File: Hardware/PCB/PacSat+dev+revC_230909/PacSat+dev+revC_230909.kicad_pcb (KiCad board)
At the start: 6 copper layers, 92 x 92 mm, 333 parts, among them J2 CONN_02X05, J801 Conn_02x05_Odd_Even, P101 U_FL, P601 U_FL, P651 Conn_04x26_Pin, P702 U_FL, P703 U_FL, Q601 SAV-331+, Q701 ATF05MS004NT1, T601 ADT4-1WT+, U156 AX5043, U2 TMS570LS0914PGE, U201 RFShield_OnePiece, U205 AX5043, U206 TLP3905, U26 DS28E83Q+T, U28 MAX31331TETB+, U29 MAX31725MTA+, U30 MAX31725MTA+, U301 RFShield_OnePiece, U305 AX5043, U401 RFShield_OnePiece, U405 AX5043, U501 RFShield_OnePiece, U505 AX5043, U602 LT6657AHMS8-2.5, U604 RBP-140+, U652 CDCLVC1106, U701 RFShield_OnePiece, U703 4n7, U705 SXBP-425+, U76 MR25H40CDE, U77 MR25H40CDE, U78 MR25H40CDE, U79 MR25H40CDE, U86 TPS7A7001DDA, U87 MAX1556AEBT+, U88 MAX1556A, U89 TPS22917DBV, U90 STWD100NYWY3F, U91 MAX4995ALAUT, U92 MAX4995ALAUT, U93 MAX4995ALAUT, U94 MAX4995ALAUT, U95 STWD100NYWY3F, Y26 AB26T-32.768KHZ-6B, Y601 588S160X2CAT

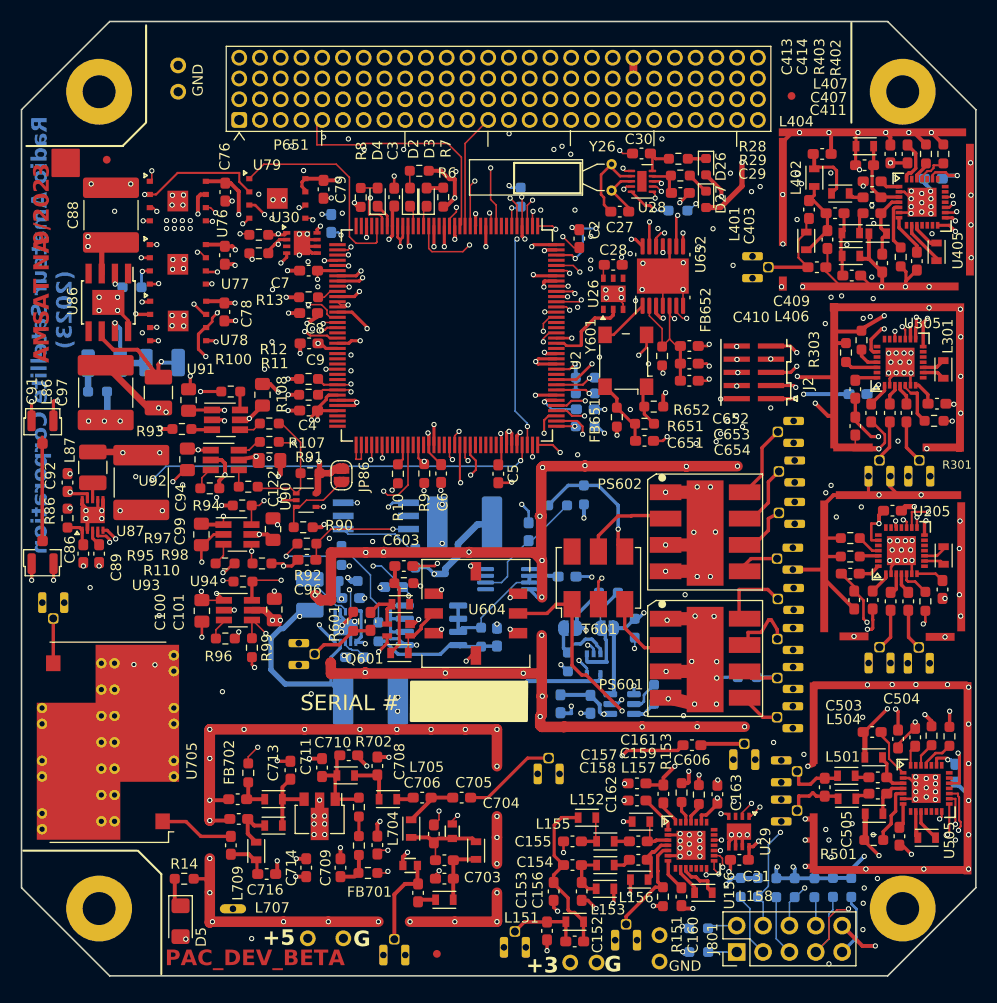
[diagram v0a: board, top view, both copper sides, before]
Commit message: Changed schematic to add Select lines for each AX5043 on the CPU.
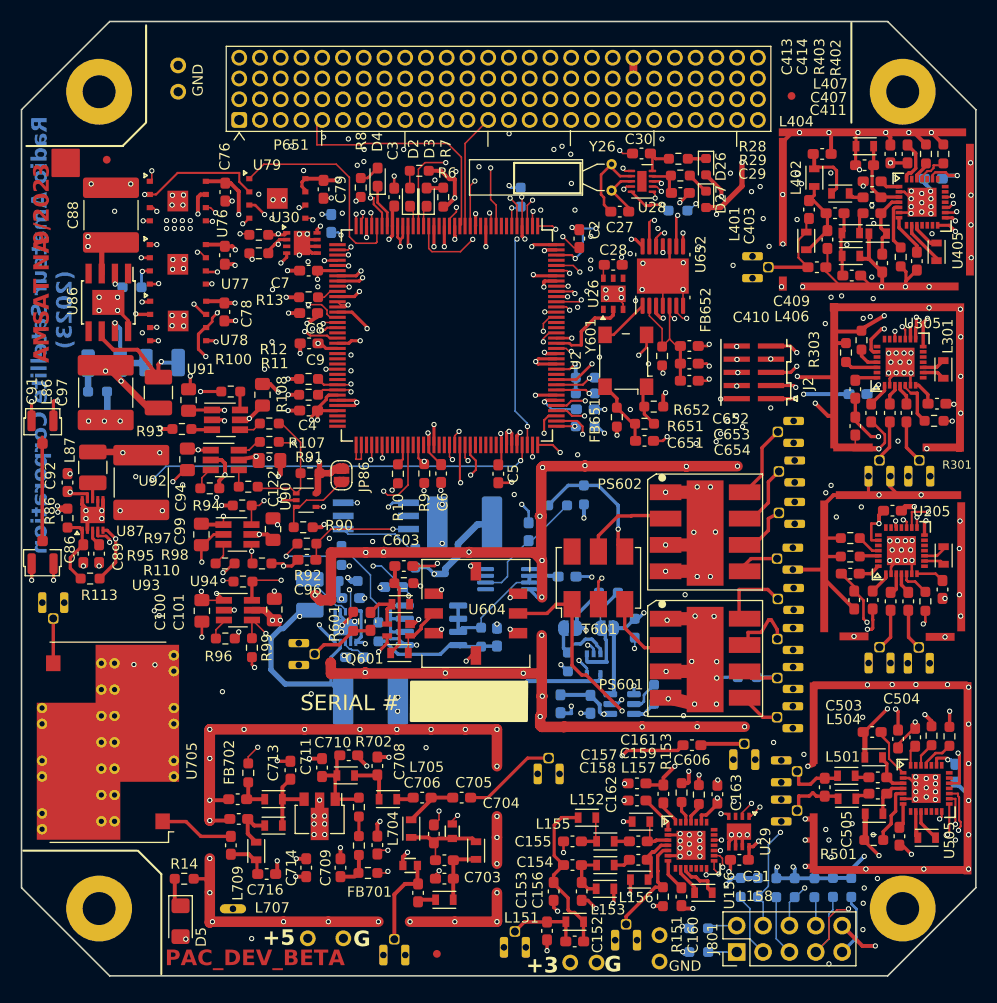
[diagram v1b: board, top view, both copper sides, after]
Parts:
- added R113: 3.8K, Resistor_SMD:R_0603_1608Metric_Pad0.98x0.95mm_HandSolder, F.Cu at (156.6, 111.7)
- moved D4 1.93 mm to (184.3, 73.0)
- moved R8 0.96 mm to (182.7, 74.0)
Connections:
- C93 pad 1: VSYS -> REG_5.0V
- J801 pad 1: AX5043_SEL_0 -> AX5043_SEL_TX
- J801 pad 3: AX5043_SEL_1 -> AX5043_SEL1
- J801 pad 5: AX5043_SEL_2 -> AX5043_SEL2
- J801 pad 7: AX5043_SEL_3 -> AX5043_SEL3
- J801 pad 9: AX5043_SEL_4 -> AX5043_SEL4
- R801 pad 2: AX5043_SEL_0 -> AX5043_SEL_TX
- R802 pad 2: AX5043_SEL_1 -> AX5043_SEL1
- R803 pad 2: AX5043_SEL_2 -> AX5043_SEL2
- R804 pad 2: AX5043_SEL_3 -> AX5043_SEL3
- R805 pad 2: AX5043_SEL_4 -> AX5043_SEL4
- R86 pad 1: VSYS -> REG_5.0V
- R87 pad 1: VSYS -> REG_5.0V
- R89 pad 2: VSYS -> REG_5.0V
- U156 pad 14: AX5043_SEL_0 -> AX5043_SEL_TX
- U2 pad 124: unconnected-(U2-N2HET1_12-Pad124) -> AX5043_SEL_TX
- U2 pad 24: unconnected-(U2-N2HET1_3-Pad24) -> AX5043_SEL1
- U2 pad 33: unconnected-(U2-N2HET1_7-Pad33) -> AX5043_SEL2
- U2 pad 35: unconnected-(U2-N2HET1_9-Pad35) -> AX5043_SEL3
- U2 pad 36: unconnected-(U2-N2HET1_4-Pad36) -> AX5043_SEL4
- U205 pad 14: AX5043_SEL_1 -> AX5043_SEL1
- U305 pad 14: AX5043_SEL_2 -> AX5043_SEL2
- U405 pad 14: AX5043_SEL_3 -> AX5043_SEL3
- U505 pad 14: AX5043_SEL_4 -> AX5043_SEL4
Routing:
- net AX5043_SEL2: track 0.00 -> 153.7 mm, vias 0 -> 7
- net AX5043_SEL4: track 0.00 -> 149.5 mm, vias 0 -> 6
- net AX5043_SEL1: track 0.00 -> 146.4 mm, vias 0 -> 6
- net AX5043_SEL3: track 0.00 -> 142.3 mm, vias 0 -> 6
- net AX5043_SEL_3: track 89.4 -> 0.00 mm, vias 3 -> 0
- net AX5043_SEL_2: track 88.7 -> 0.00 mm, vias 3 -> 0
- net AX5043_SEL_TX: track 0.00 -> 69.6 mm, vias 0 -> 2
- net AX5043_SEL_1: track 67.3 -> 0.00 mm, vias 3 -> 0
- net VSYS: track 90.5 -> 43.8 mm, vias 8 -> 4
- net REG_5.0V: track 43.7 -> 87.4 mm, vias 5 -> 10
- net AX5043_SEL_4: track 30.2 -> 0.00 mm, vias 2 -> 0
- net AX5043_SEL_0: track 12.0 -> 0.00 mm, vias 1 -> 0
- net HW_POWER_OFF_N: track 94.6 -> 100.6 mm
- net Net-(U87-IN): track 2.97 -> 7.16 mm
- net Net-(D4-K): track 2.30 -> 4.23 mm
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- removed copper zone on In2.Cu, net GND
